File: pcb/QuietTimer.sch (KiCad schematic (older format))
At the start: 4 parts

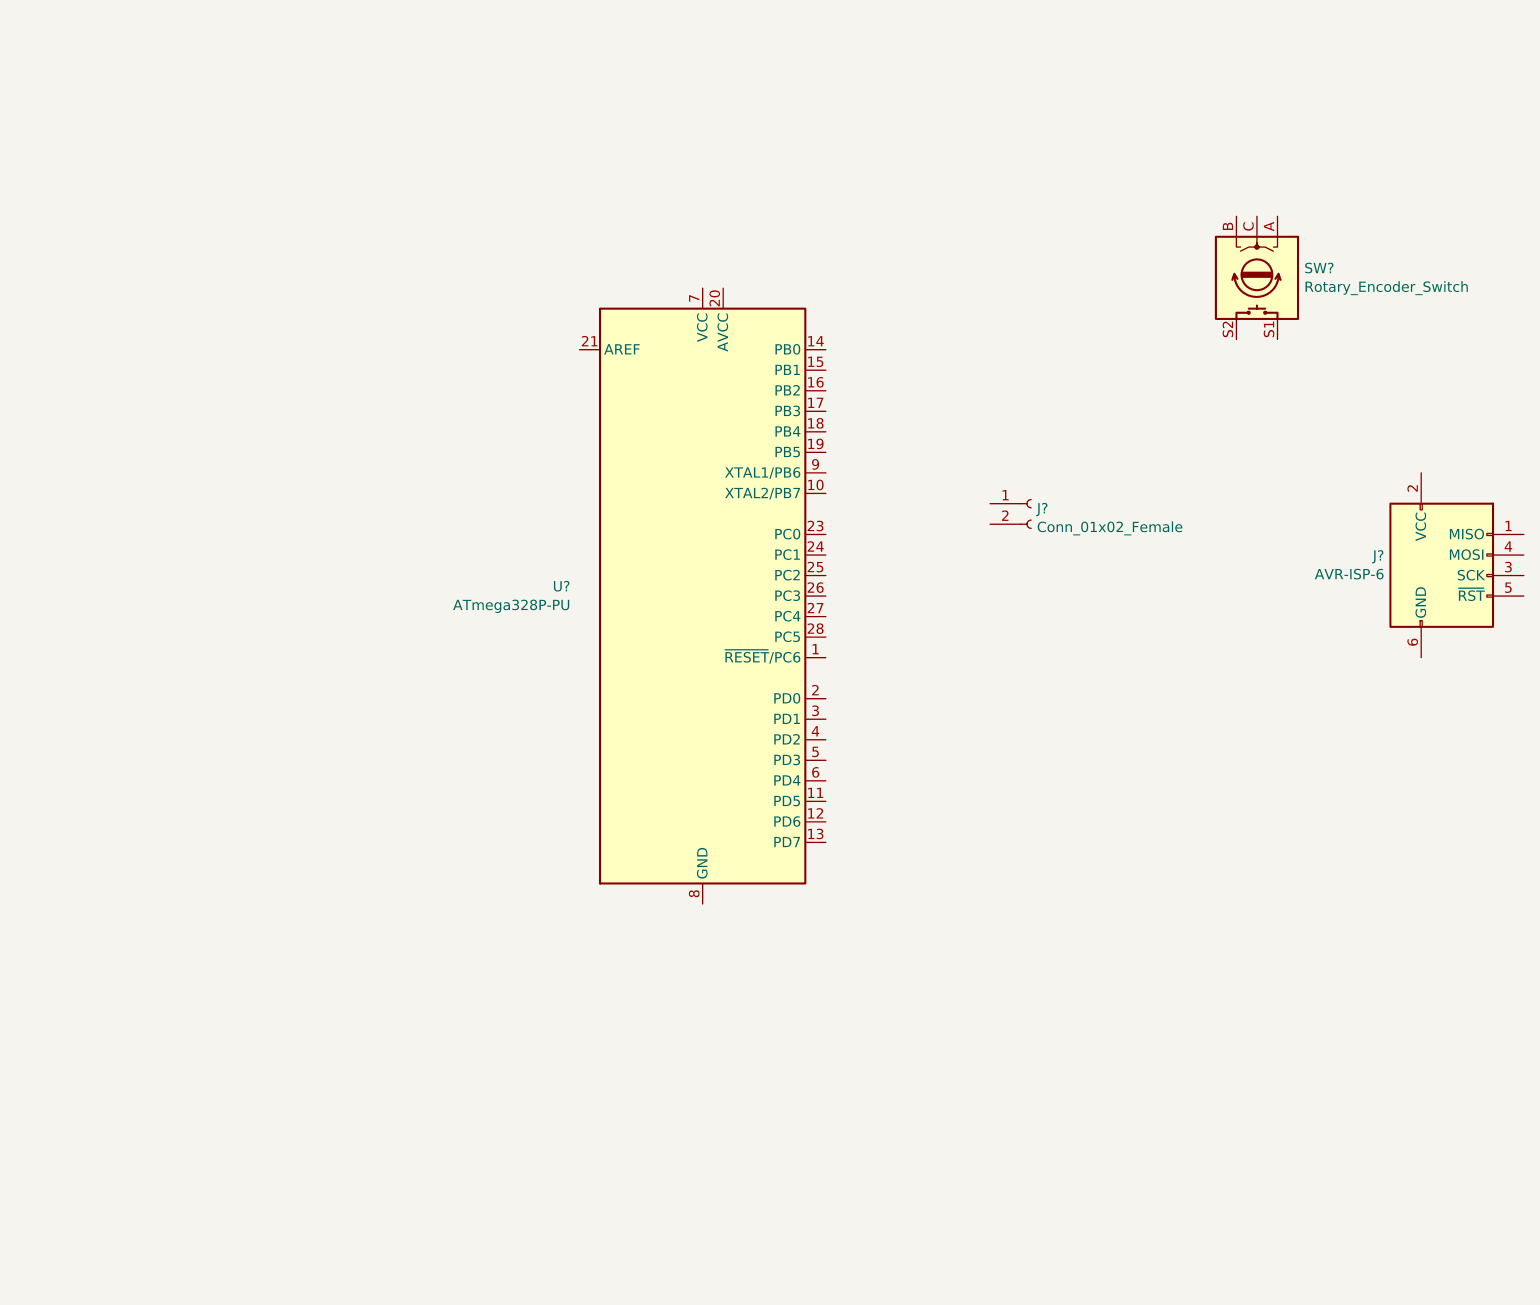
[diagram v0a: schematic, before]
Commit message: Finish Custom Footprints
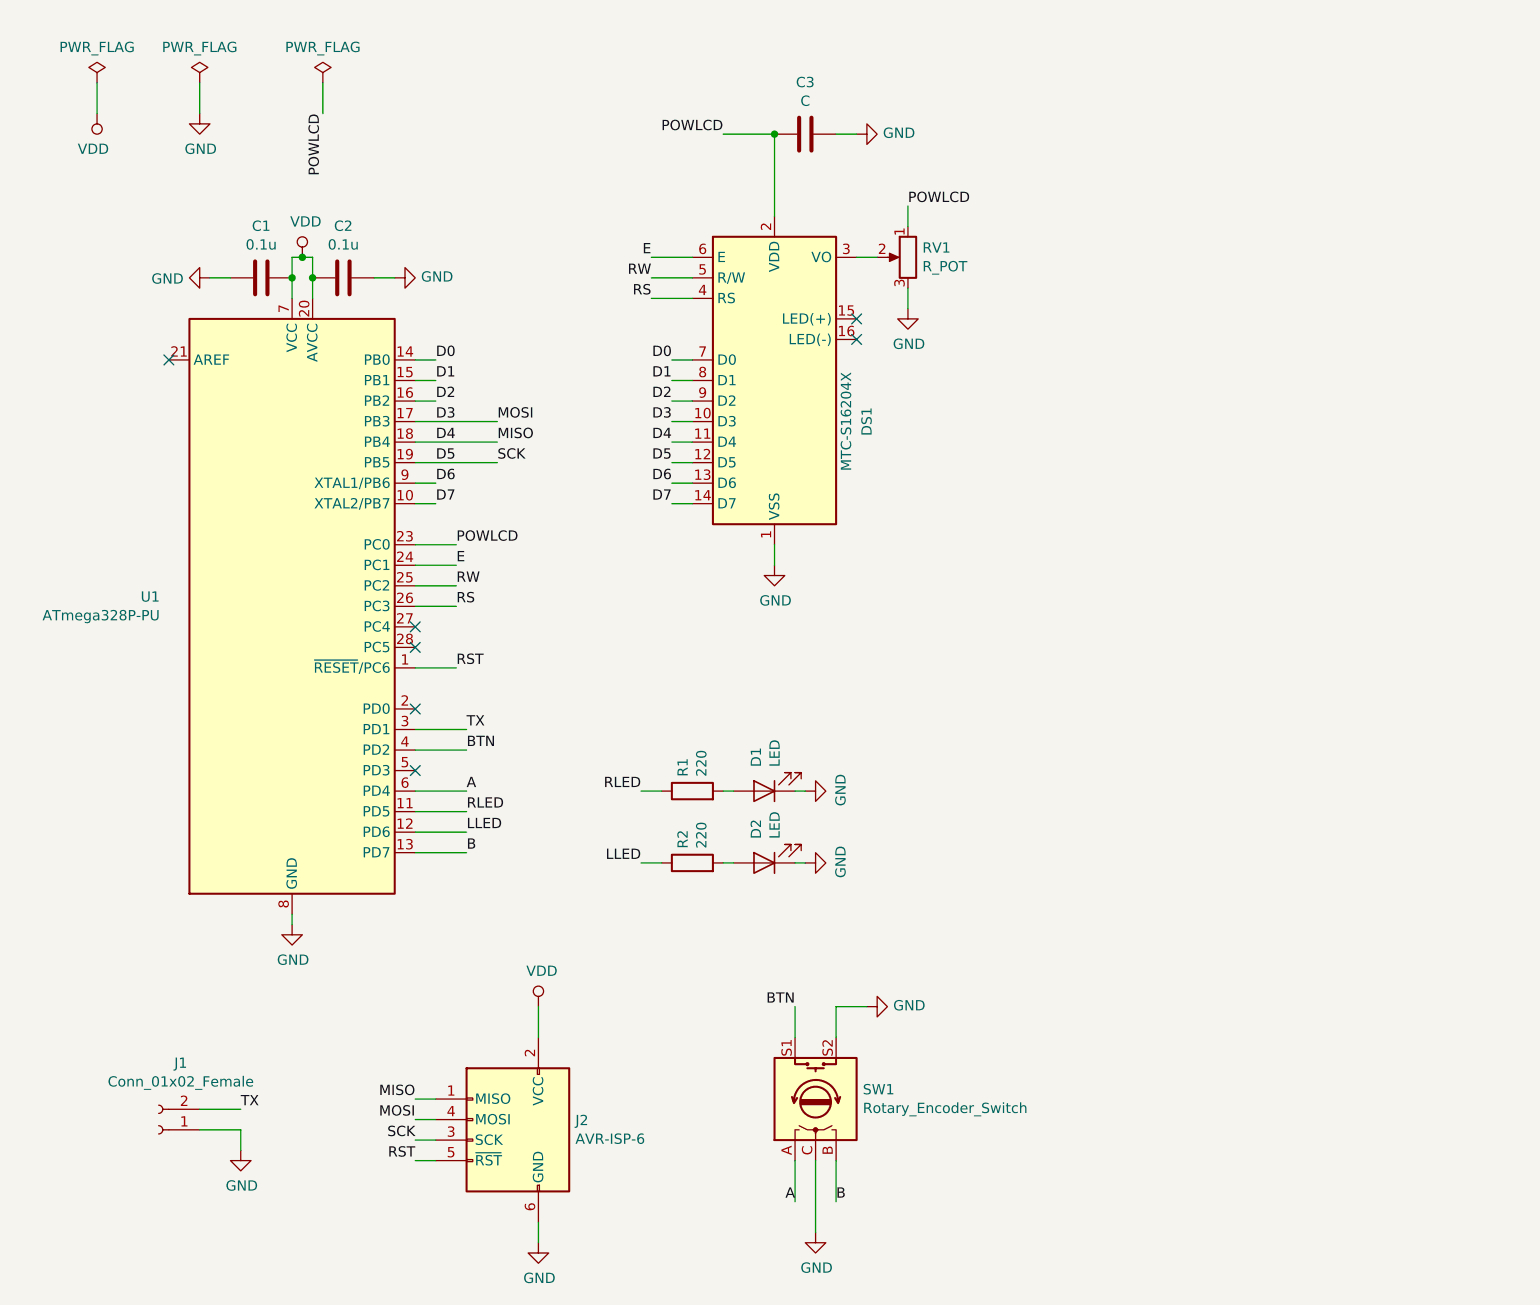
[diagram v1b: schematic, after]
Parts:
- removed J?: AVR-ISP-6, symbol Connector:AVR-ISP-6
- removed J?: Conn_01x02_Female, symbol Connector:Conn_01x02_Female
- removed SW?: Rotary_Encoder_Switch, symbol Device:Rotary_Encoder_Switch
- removed U?: ATmega328P-PU, Package_DIP:DIP-28_W7.62mm, symbol MCU_Microchip_ATmega:ATmega328P-PU
- added C1, C2: 0.1u, symbol Device:C
- added C3: C, symbol Device:C
- added D1, D2: LED, symbol Device:LED
- added DS1: MTC-S16204X, Display:WC1602A, symbol lcd:MTC-S16204X
- added J1: Conn_01x02_Female, symbol Connector:Conn_01x02_Female
- added J2: AVR-ISP-6, symbol Connector:AVR-ISP-6
- added R1, R2: 220, symbol Device:R
- added RV1: R_POT, symbol Device:R_POT
- added SW1: Rotary_Encoder_Switch, symbol Device:Rotary_Encoder_Switch
- added U1: ATmega328P-PU, Package_DIP:DIP-28_W7.62mm, symbol MCU_Microchip_ATmega:ATmega328P-PU
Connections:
- new net: DS1.3 (VO), RV1.2
- new net: D1.2 (A), R1.2
- new net: D2.2 (A), R2.2
- new net A: SW1.A, U1.6 (PD4)
- new net B: SW1.B, U1.13 (PD7)
- new net BTN: SW1.S1, U1.4 (PD2)
- new net D0: DS1.7 (D0), U1.14 (PB0)
- new net D1: DS1.8 (D1), U1.15 (PB1)
- new net D2: DS1.9 (D2), U1.16 (PB2)
- new net D3: DS1.10 (D3), J2.4 (MOSI), U1.17 (PB3)
- new net D4: DS1.11 (D4), J2.1 (MISO), U1.18 (PB4)
- new net D5: DS1.12 (D5), J2.3 (SCK), U1.19 (PB5)
- new net D6: DS1.13 (D6), U1.9 (XTAL1/PB6)
- new net D7: DS1.14 (D7), U1.10 (XTAL2/PB7)
- new net E: DS1.6 (E), U1.24 (PC1)
- new net GND: C1.2, C2.1, C3.1, D1.1 (K), D2.1 (K), DS1.1 (VSS), J1.1 (Pin_1), J2.6 (GND), RV1.3, SW1.C, SW1.S2, U1.22 (GND), U1.8 (GND)
- new net LLED: R2.1, U1.12 (PD6)
- new net POWLCD: C3.2, DS1.2 (VDD), RV1.1, U1.23 (PC0)
- new net RLED: R1.1, U1.11 (PD5)
- new net RS: DS1.4 (RS), U1.26 (PC3)
- new net RST: J2.5 (~RST), U1.1 (~RESET~/PC6)
- new net RW: DS1.5 (R/W), U1.25 (PC2)
- new net TX: J1.2 (Pin_2), U1.3 (PD1)
- new net VDD: C1.1, C2.2, J2.2 (VCC), U1.20 (AVCC), U1.7 (VCC)
- no-connect marks 0 -> 7

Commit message: Finished Schematic
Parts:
- added C4: 10u, Capacitor_THT:CP_Radial_D5.0mm_P2.00mm, symbol Device:CP
- added J3: Conn_01x02, Connector_Wire:SolderWirePad_1x02_P3.81mm_Drill0.8mm, symbol Connector_Generic:Conn_01x02
- C1, C2: footprint (none) -> Capacitor_THT:C_Disc_D5.0mm_W2.5mm_P2.50mm
- C3: value C -> 0.1u; footprint (none) -> Capacitor_THT:C_Disc_D5.0mm_W2.5mm_P2.50mm
- D1, D2: footprint (none) -> LED_THT:LED_D3.0mm
- DS1: footprint Display:WC1602A -> lcd:MTC-16204X
- J1: footprint (none) -> Connector_PinSocket_2.54mm:PinSocket_1x02_P2.54mm_Vertical
- J2: footprint (none) -> Connector_IDC:IDC-Header_2x03_P2.54mm_Vertical
- R1, R2: footprint (none) -> Resistor_THT:R_Axial_DIN0207_L6.3mm_D2.5mm_P2.54mm_Vertical
- RV1: footprint (none) -> Potentiometer_THT:Potentiometer_Piher_PT-6-V_Vertical_Hole
- SW1: footprint (none) -> Connector_PinHeader_2.54mm:PinHeader_1x05_P2.54mm_Vertical
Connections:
- net GND: now also C4.2, J3.2 (Pin_2)
- net VDD: now also C4.1, J3.1 (Pin_1)
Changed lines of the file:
@@
 F 0 "J2" H 2670 6146 50  0000 R CNN
 F 1 "AVR-ISP-6" H 2670 6055 50  0000 R CNN
-F 2 "" V 2700 6100 50  0001 C CNN
+F 2 "Connector_IDC:IDC-Header_2x03_P2.54mm_Vertical" V 2700 6100 50  0001 C CNN
 F 3 " ~" H 1675 5500 50  0001 C CNN
 	1    2950 6050
@@
 F 0 "J1" H 1092 5675 50  0000 C CNN
 F 1 "Conn_01x02_Female" H 1092 5766 50  0000 C CNN
-F 2 "" H 1200 6000 50  0001 C CNN
+F 2 "Connector_PinSocket_2.54mm:PinSocket_1x02_P2.54mm_Vertical" H 1200 6000 50  0001 C CNN
 F 3 "~" H 1200 6000 50  0001 C CNN
 	1    1200 6000
@@
 F 0 "SW1" V 4446 5620 50  0000 R CNN
 F 1 "Rotary_Encoder_Switch" V 4355 5620 50  0000 R CNN
-F 2 "" H 4250 6010 50  0001 C CNN
+F 2 "Connector_PinHeader_2.54mm:PinHeader_1x05_P2.54mm_Vertical" H 4250 6010 50  0001 C CNN
 F 3 "~" H 4400 6110 50  0001 C CNN
 	1    4400 5850
@@
 F 0 "C2" V 1848 1850 50  0000 C CNN
 F 1 "0.1u" V 1939 1850 50  0000 C CNN
-F 2 "" H 2138 1700 50  0001 C CNN
+F 2 "Capacitor_THT:C_Disc_D5.0mm_W2.5mm_P2.50mm" H 2138 1700 50  0001 C CNN
 F 3 "~" H 2100 1850 50  0001 C CNN
 	1    2100 1850
@@
 F 0 "C1" V 1448 1850 50  0000 C CNN
 F 1 "0.1u" V 1539 1850 50  0000 C CNN
-F 2 "" H 1738 1700 50  0001 C CNN
+F 2 "Capacitor_THT:C_Disc_D5.0mm_W2.5mm_P2.50mm" H 1738 1700 50  0001 C CNN
 F 3 "~" H 1700 1850 50  0001 C CNN
 	1    1700 1850
@@
 F 0 "R2" H 3870 4746 50  0000 L CNN
 F 1 "220" H 3870 4655 50  0000 L CNN
-F 2 "" V 3730 4700 50  0001 C CNN
+F 2 "Resistor_THT:R_Axial_DIN0207_L6.3mm_D2.5mm_P2.54mm_Vertical" V 3730 4700 50  0001 C CNN
 F 3 "~" H 3800 4700 50  0001 C CNN
 	1    3800 4700
@@
 F 0 "R1" H 3870 4396 50  0000 L CNN
 F 1 "220" H 3870 4305 50  0000 L CNN
-F 2 "" V 3730 4350 50  0001 C CNN
+F 2 "Resistor_THT:R_Axial_DIN0207_L6.3mm_D2.5mm_P2.54mm_Vertical" V 3730 4350 50  0001 C CNN
 F 3 "~" H 3800 4350 50  0001 C CNN
 	1    3800 4350
@@
 F 0 "D2" V 4189 4583 50  0000 R CNN
 F 1 "LED" V 4098 4583 50  0000 R CNN
-F 2 "" H 4150 4700 50  0001 C CNN
+F 2 "LED_THT:LED_D3.0mm" H 4150 4700 50  0001 C CNN
 F 3 "~" H 4150 4700 50  0001 C CNN
 	1    4150 4700
@@
 F 0 "D1" V 4189 4233 50  0000 R CNN
 F 1 "LED" V 4098 4233 50  0000 R CNN
-F 2 "" H 4150 4350 50  0001 C CNN
+F 2 "LED_THT:LED_D3.0mm" H 4150 4350 50  0001 C CNN
 F 3 "~" H 4150 4350 50  0001 C CNN
 	1    4150 4350
@@
 F 0 "DS1" V 4650 2150 50  0000 C CNN
 F 1 "MTC-S16204X" V 4550 2150 50  0000 C CNN
-F 2 "Display:WC1602A" H 4200 1450 50  0001 C CIN
+F 2 "lcd:MTC-16204X" H 4200 1450 50  0001 C CIN
 F 3 "http://www.wincomlcd.com/pdf/WC1602A-SFYLYHTC06.pdf" H 4900 2350 50  0001 C CNN
 	1    4200 2350
@@
 P 4350 1150
 F 0 "C3" V 4098 1150 50  0000 C CNN
-F 1 "C" V 4189 1150 50  0000 C CNN
-F 2 "" H 4388 1000 50  0001 C CNN
+F 1 "0.1u" V 4189 1150 50  0000 C CNN
+F 2 "Capacitor_THT:C_Disc_D5.0mm_W2.5mm_P2.50mm" H 4388 1000 50  0001 C CNN
 F 3 "~" H 4350 1150 50  0001 C CNN
 	1    4350 1150
@@
 F 0 "RV1" H 4780 1796 50  0000 R CNN
 F 1 "R_POT" H 4780 1705 50  0000 R CNN
-F 2 "" H 4850 1750 50  0001 C CNN
+F 2 "Potentiometer_THT:Potentiometer_Piher_PT-6-V_Vertical_Hole" H 4850 1750 50  0001 C CNN
 F 3 "~" H 4850 1750 50  0001 C CNN
 	1    4850 1750
@@
 Wire Wire Line
 	2000 900  2000 1050
+$Comp
+L Connector_Generic:Conn_01x02 J3
+U 1 1 5E484B35
+P 2550 950
+F 0 "J3" H 2468 1167 50  0000 C CNN
+F 1 "Conn_01x02" H 2468 1076 50  0000 C CNN
+F 2 "Connector_Wire:SolderWirePad_1x02_P3.81mm_Drill0.8mm" H 2550 950 50  0001 C CNN
+F 3 "~" H 2550 950 50  0001 C CNN
+	1    2550 950
+	-1   0    0    -1
+$EndComp
+$Comp
+L power:VDD #PWR017
+U 1 1 5E48697B
+P 3000 800
+F 0 "#PWR017" H 3000 650 50  0001 C CNN
+F 1 "VDD" H 3017 973 50  0000 C CNN
+F 2 "" H 3000 800 50  0001 C CNN
+F 3 "" H 3000 800 50  0001 C CNN
+	1    3000 800
+	1    0    0    -1
+$EndComp
+$Comp
+L power:GND #PWR018
+U 1 1 5E487274
+P 3000 1300
+F 0 "#PWR018" H 3000 1050 50  0001 C CNN
+F 1 "GND" H 3005 1127 50  0000 C CNN
+F 2 "" H 3000 1300 50  0001 C CNN
+F 3 "" H 3000 1300 50  0001 C CNN
+	1    3000 1300
+	1    0    0    -1
+$EndComp
+Wire Wire Line
+	2750 950  3000 950
+Wire Wire Line
+	2750 1050 3000 1050
+$Comp
+L Device:CP C4
+U 1 1 5E487619
+P 3250 1000
+F 0 "C4" H 3368 1046 50  0000 L CNN
+F 1 "10u" H 3368 955 50  0000 L CNN
+F 2 "Capacitor_THT:CP_Radial_D5.0mm_P2.00mm" H 3288 850 50  0001 C CNN
+F 3 "~" H 3250 1000 50  0001 C CNN
+	1    3250 1000
+	1    0    0    -1
+$EndComp
+Wire Wire Line
+	3000 800  3000 850
+Wire Wire Line
+	3000 1050 3000 1150
+Wire Wire Line
+	3250 850  3000 850
+Connection ~ 3000 850
+Wire Wire Line
+	3000 850  3000 950
+Wire Wire Line
+	3250 1150 3000 1150
+Connection ~ 3000 1150
+Wire Wire Line
+	3000 1150 3000 1300
 $EndSCHEMATC

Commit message: Finished PCB
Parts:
- removed SW1: Rotary_Encoder_Switch, Connector_PinHeader_2.54mm:PinHeader_1x05_P2.54mm_Vertical, symbol Device:Rotary_Encoder_Switch
- added J4: Conn_01x05_Male, Connector_PinHeader_2.54mm:PinHeader_1x05_P2.54mm_Vertical, symbol Connector:Conn_01x05_Male
- added J5: USB_B_Micro, Connector_USB:USB_Micro-B_Wuerth_614105150721_Vertical, symbol Connector:USB_B_Micro
- RV1: value R_POT -> 10k
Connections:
- net A: now also U1.5 (PD3), J4.3 (Pin_3); no longer U1.6 (PD4)
- net B: now also U1.6 (PD4), J4.5 (Pin_5); no longer U1.13 (PD7)
- net BTN: now also J4.1 (Pin_1)
- net GND: now also J4.2 (Pin_2), J4.4 (Pin_4), J5.5 (GND), J5.6 (Shield)
- net VDD: now also J5.1 (VBUS)
- no-connect marks 7 -> 10
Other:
- moved on the sheet: C3, D1, D2, DS1, R1, R2, RV1
